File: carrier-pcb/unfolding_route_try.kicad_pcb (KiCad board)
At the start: 2 copper layers, 66 parts, among them J1 USB_C_Receptacle_USB2.0, J2 Conn_01x04_Female, J3 CONN_1-338068-8_TYC, U1 TCA9548APWR, U10 DRV2605LDGS, U11 DRV2605LDGS, U12 BMX160, U2 TCA9548APWR, U3 DRV2605LDGS, U4 DRV2605LDGS, U5 DRV2605LDGS, U6 DRV2605LDGS, U7 DRV2605LDGS, U8 DRV2605LDGS, U9 DRV2605LDGS

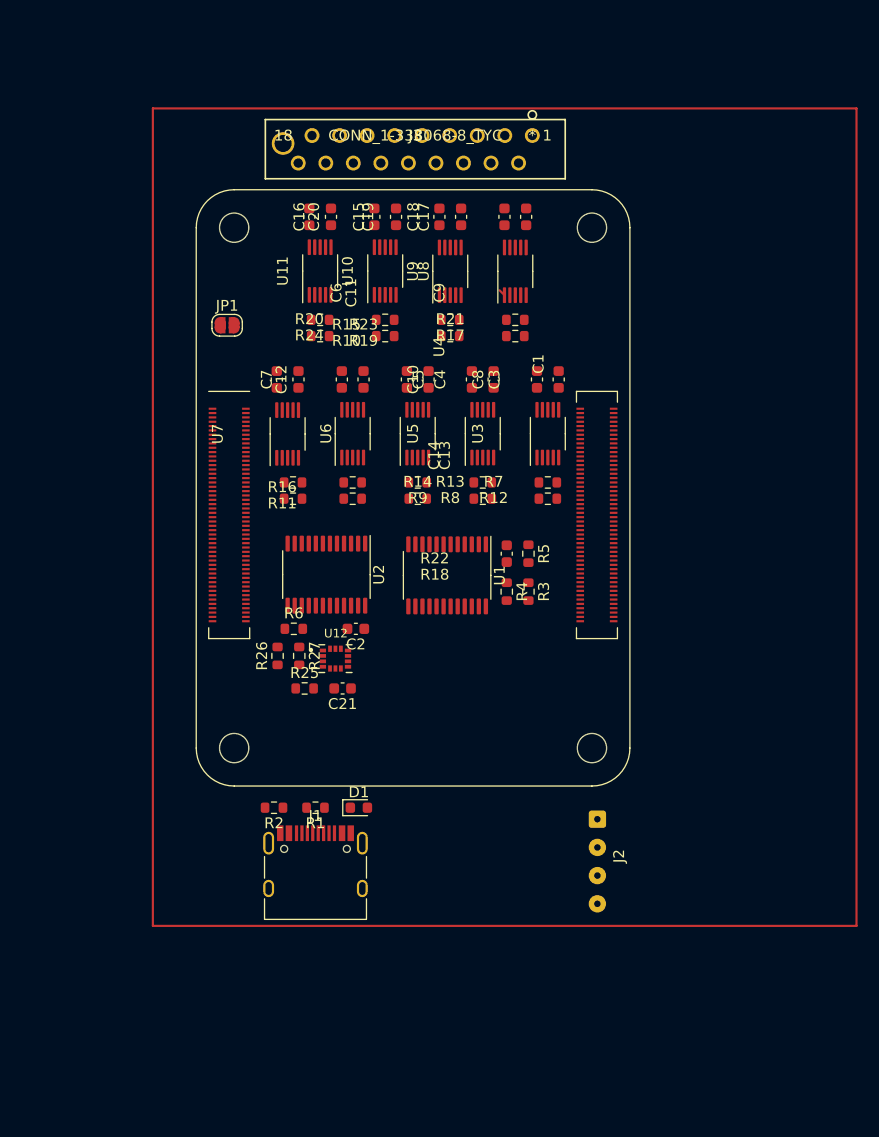
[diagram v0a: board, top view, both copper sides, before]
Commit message: Add 3rd_party_libs folder and place footrpints and symbols. Place bmx160 and TE IDC connector. Add route_try file to try out routing.
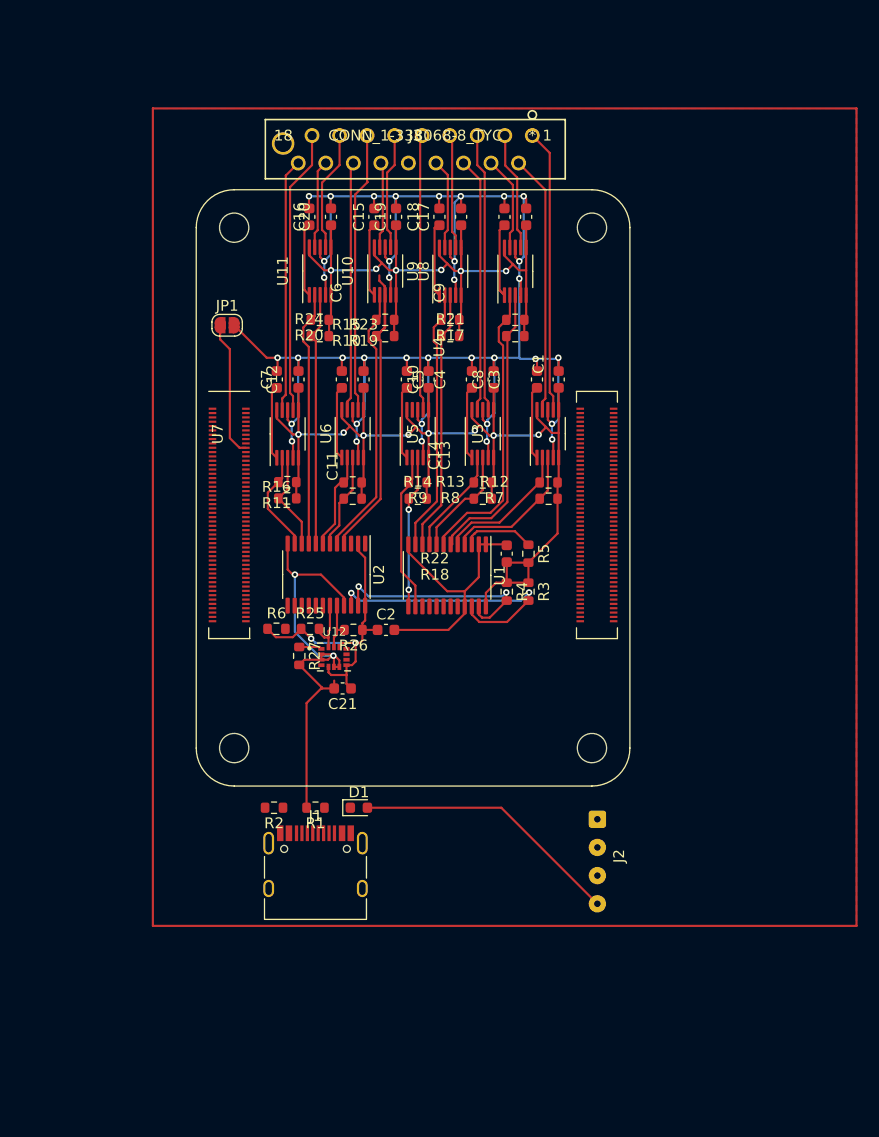
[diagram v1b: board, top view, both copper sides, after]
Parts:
- moved R26 7.40 mm to (130.0, 76.1), turned to 180 degrees
- moved R25 5.52 mm to (126.0, 76.0)
- moved C2 2.78 mm to (133.0, 76.1), turned to 0 degrees
- moved R6 1.60 mm to (122.9, 76.0)
- moved R12 1.50 mm to (148.0, 62.5)
- moved R7 1.50 mm to (148.0, 64.0)
- moved R20 1.50 mm to (126.9, 49.0)
- moved R24 1.50 mm to (126.9, 47.5)
- moved R11 0.53 mm to (123.9, 64.0)
- moved R16 0.53 mm to (123.9, 62.5)
- moved U12 0.21 mm to (128.2, 78.6)
- turned C11 to 90 degrees
- turned C12 to 90 degrees
- turned C19 to 90 degrees
- turned C20 to 90 degrees
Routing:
- net GND: track 0.00 -> 252.3 mm, vias 0 -> 38
- net +3V3: track 0.00 -> 208.9 mm, vias 0 -> 16
- net SDA6: track 0.00 -> 31.0 mm
- net SCL2: track 0.00 -> 27.1 mm
- net SDA2: track 0.00 -> 26.8 mm
- net M9+: track 0.00 -> 26.3 mm
- net M1+: track 0.00 -> 26.1 mm
- net SCL: track 0.00 -> 26.0 mm, vias 0 -> 2
- net M7+: track 0.00 -> 25.9 mm
- net M3+: track 0.00 -> 25.7 mm
- net M5+: track 0.00 -> 25.5 mm
- net SCL6: track 0.00 -> 25.2 mm
- net +5V: track 0.00 -> 24.9 mm
- net SCL4: track 0.00 -> 24.4 mm
- net SDA4: track 0.00 -> 24.0 mm
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- added copper zone on B.Cu, net GND

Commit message: Route everything in route_try file
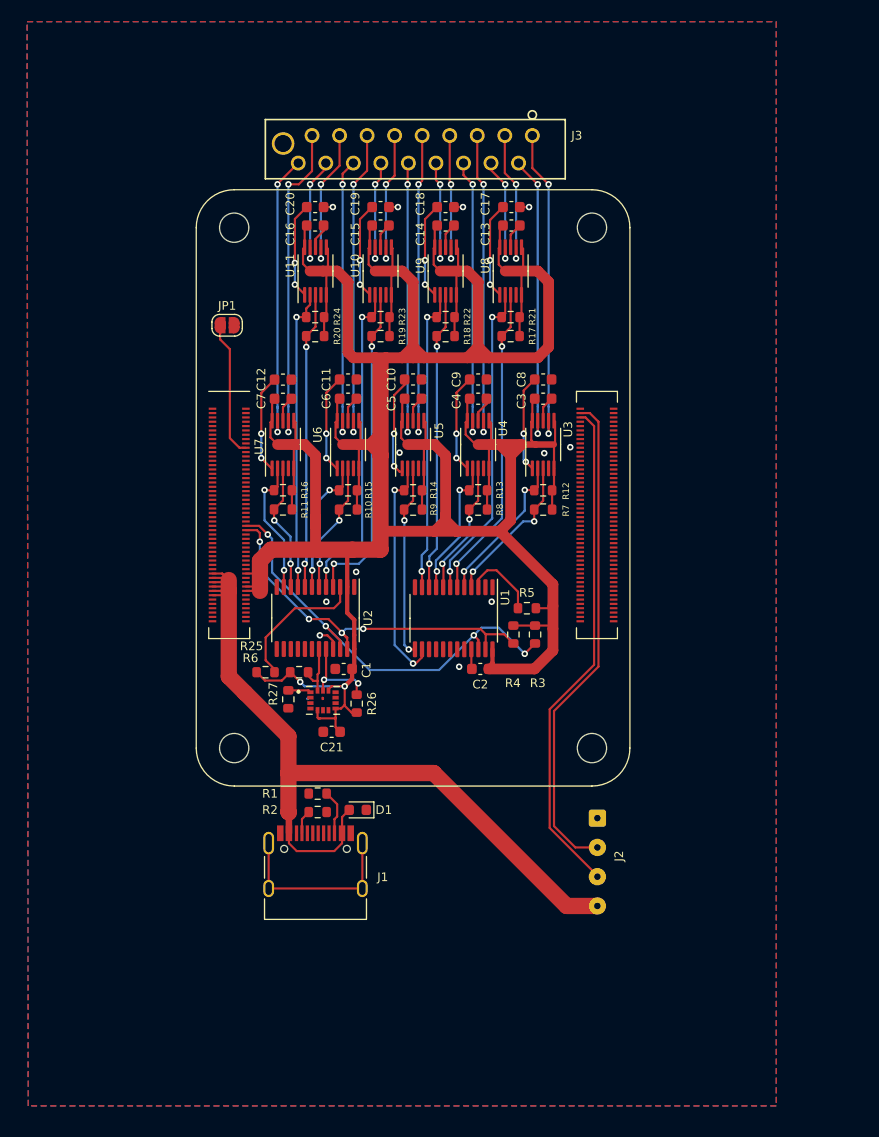
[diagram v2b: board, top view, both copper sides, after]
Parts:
- J3: value CONN_1-338068-8_TYC -> 1-338068-8
- moved C1 18.4 mm to (129.1, 79.7), turned to 180 degrees
- moved C2 9.42 mm to (141.7, 79.7), turned to 180 degrees
- moved R26 6.81 mm to (130.3, 82.9), turned to 90 degrees
- moved R5 5.03 mm to (146.0, 74.1), turned to 180 degrees
- moved C21 4.12 mm to (128.0, 85.5)
- moved R25 4.12 mm to (125.0, 80.0)
- moved R27 4.12 mm to (124.0, 82.5)
- moved R6 4.12 mm to (121.9, 80.0)
- moved U2 4.12 mm to (126.5, 75.0)
- moved U12 4.12 mm to (127.2, 82.6)
- moved R2 4.04 mm to (126.7, 92.9), turned to 0 degrees
- moved R3 4.00 mm to (146.8, 76.5)
- moved R4 4.00 mm to (144.8, 76.5)
- moved U1 4.00 mm to (139.2, 75.0)
- moved C7 2.29 mm to (123.5, 54.8), turned to 0 degrees
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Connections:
- U5 pad 9: M5-. -> M5-
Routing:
- net GND: track 252.3 -> 28.7 mm, vias 38 -> 12
- net +3V3: track 208.9 -> 342.2 mm, vias 16 -> 2
- net +5V: track 24.9 -> 78.8 mm
- net USB_D+: track 0.00 -> 46.6 mm
- net USB_D-: track 0.00 -> 45.8 mm
- net M5-: track 0.00 -> 25.9 mm, vias 0 -> 2
- net unconnected-(J1-PadS1): track 0.00 -> 17.0 mm
- net SCL: track 26.0 -> 41.2 mm, vias 2 -> 4
- net SDA: track 20.8 -> 35.1 mm, vias 2 -> 4
- net Net-(R6-Pad2): track 0.00 -> 13.2 mm
- net SCL7: track 9.05 -> 18.1 mm, vias 0 -> 2
- net SCL5: track 14.7 -> 21.5 mm, vias 0 -> 2
- net SCL6: track 25.2 -> 30.4 mm, vias 0 -> 2
- net SDA8: track 23.5 -> 28.3 mm, vias 0 -> 2
- net SCL8: track 23.6 -> 28.1 mm, vias 0 -> 2
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- added copper zone on F.Cu, net GND

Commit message: New routing
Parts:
- added J4: Conn_01x01_Female, Connector_Wire:SolderWirePad_1x01_SMD_1x2mm, F.Cu at (146.1, 89.0)
- added J5: Conn_01x01_Female, Connector_Wire:SolderWirePad_1x01_SMD_1x2mm, F.Cu at (147.5, 89.0)
- added J6: Conn_01x01_Female, Connector_Wire:SolderWirePad_1x01_SMD_1x2mm, F.Cu at (142.7, 89.0)
- J2: value Conn_01x04_Female -> Conn_01x01_Female; footprint Connector_Wire:SolderWire-0.1sqmm_1x04_P3.6mm_D0.4mm_OD1mm -> Connector_Wire:SolderWirePad_1x01_SMD_1x2mm
- moved C21 15.8 mm to (143.8, 84.8), turned to -90 degrees
- moved U12 14.0 mm to (141.0, 84.9)
- moved R27 13.7 mm to (137.6, 84.1), turned to 180 degrees
- moved R25 12.8 mm to (137.6, 82.6)
- moved R6 12.5 mm to (129.8, 70.2), turned to 180 degrees
- moved R26 10.4 mm to (140.7, 82.6), turned to 180 degrees
- moved J2 8.78 mm to (144.1, 89.0), turned to 180 degrees
- moved R2 2.50 mm to (124.2, 92.8), turned to 180 degrees
- moved R1 2.50 mm to (124.2, 91.3)
- moved D1 1.56 mm to (128.9, 92.1), turned to -90 degrees
- moved JP1 1.17 mm to (119.2, 48.8)
- moved C17 0.30 mm to (144.6, 36.8)
- moved C18 0.30 mm to (138.5, 36.8)
- moved C19 0.30 mm to (132.5, 36.8)
- moved C20 0.30 mm to (126.5, 36.8)
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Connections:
- J2 pad 1: GND -> +5V
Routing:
- net USB_D+: track 46.6 -> 0.00 mm
- net USB_D-: track 45.8 -> 0.00 mm
- net +3V3: track 342.2 -> 366.8 mm
- net GND: track 28.7 -> 49.8 mm, vias 12 -> 75
- net +5V: track 78.8 -> 62.1 mm
- net SDA_bmx160: track 5.28 -> 18.8 mm
- net Net-(R6-Pad2): track 13.2 -> 1.95 mm
- net SCL_bmx160: track 8.33 -> 19.2 mm, vias 2 -> 0
- net SCL7: track 18.1 -> 12.3 mm, vias 2 -> 0
- net SDA: track 35.1 -> 38.5 mm
- net SCL: track 41.2 -> 39.0 mm
- net SCL1: track 15.1 -> 13.8 mm, vias 2 -> 0
- net SDA2: track 29.1 -> 30.2 mm
- net Net-(J1-PadB5): track 4.16 -> 5.24 mm
- net SDA4: track 27.6 -> 28.6 mm
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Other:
- board outline added: 57 x 78.5 mm

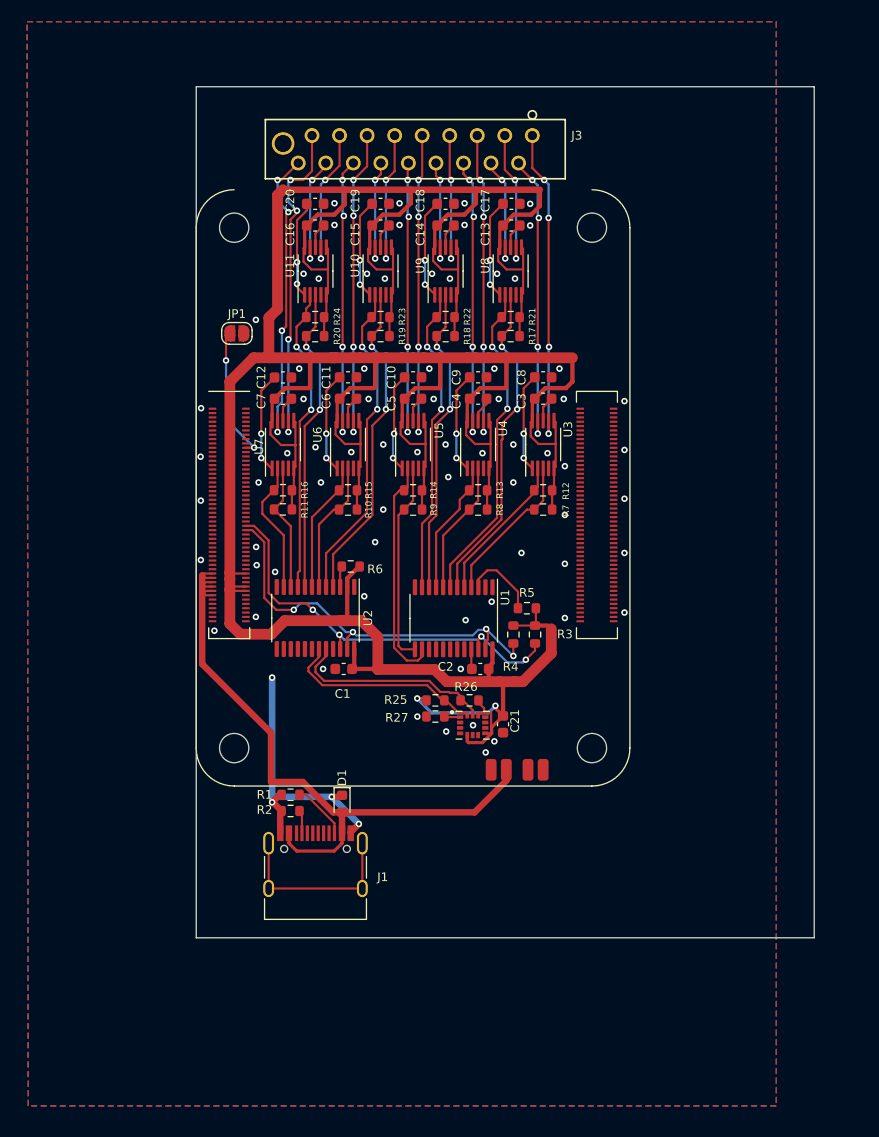
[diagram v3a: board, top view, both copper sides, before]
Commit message: finish new routing with diff pair. export stp file.
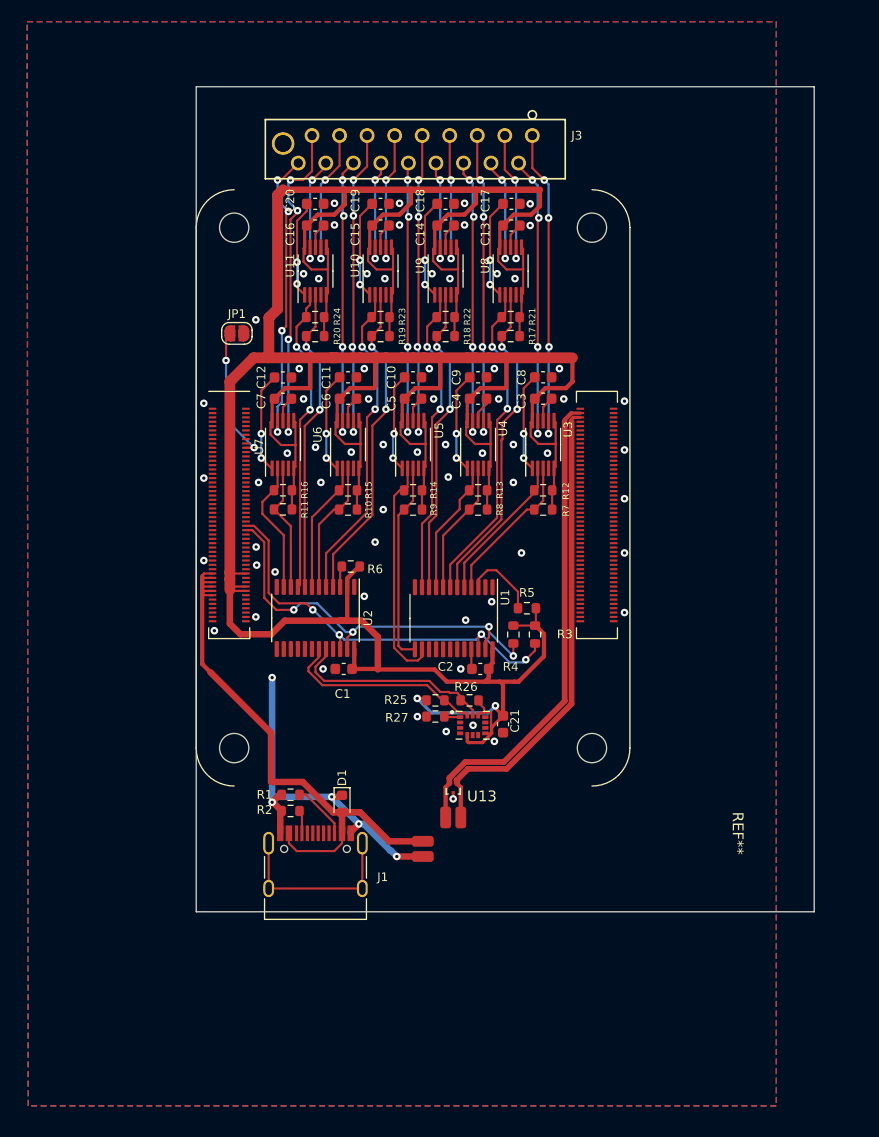
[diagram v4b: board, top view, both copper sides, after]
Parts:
- added REF**: SteckerMicro-USB30-gewinkelt, own:SteckerMicro-USB30-gewinkelt, F.Cu at (164.9, 94.9)
- added U13: TPD2EUSB30, Package_TO_SOT_SMD:Texas_DRT-3, F.Cu at (139.2, 90.7)
- moved J6 10.2 mm to (136.4, 97.0), turned to -90 degrees
- moved J2 10.1 mm to (136.4, 95.6), turned to -90 degrees
- moved J5 10.0 mm to (138.5, 93.4), turned to 0 degrees
- moved J4 7.60 mm to (139.9, 93.4), turned to 0 degrees
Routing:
- net USB_D-: track 0.00 -> 44.9 mm
- net USB_D+: track 0.00 -> 44.1 mm
- net +5V: track 62.1 -> 53.3 mm
- net GND: track 49.8 -> 57.6 mm, vias 75 -> 71
- net +3V3: track 366.8 -> 364.7 mm
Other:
- board size 57 x 78.5 mm -> 57 x 76.1 mm

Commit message: reroute usb traces. make motor traces thicker. small changes
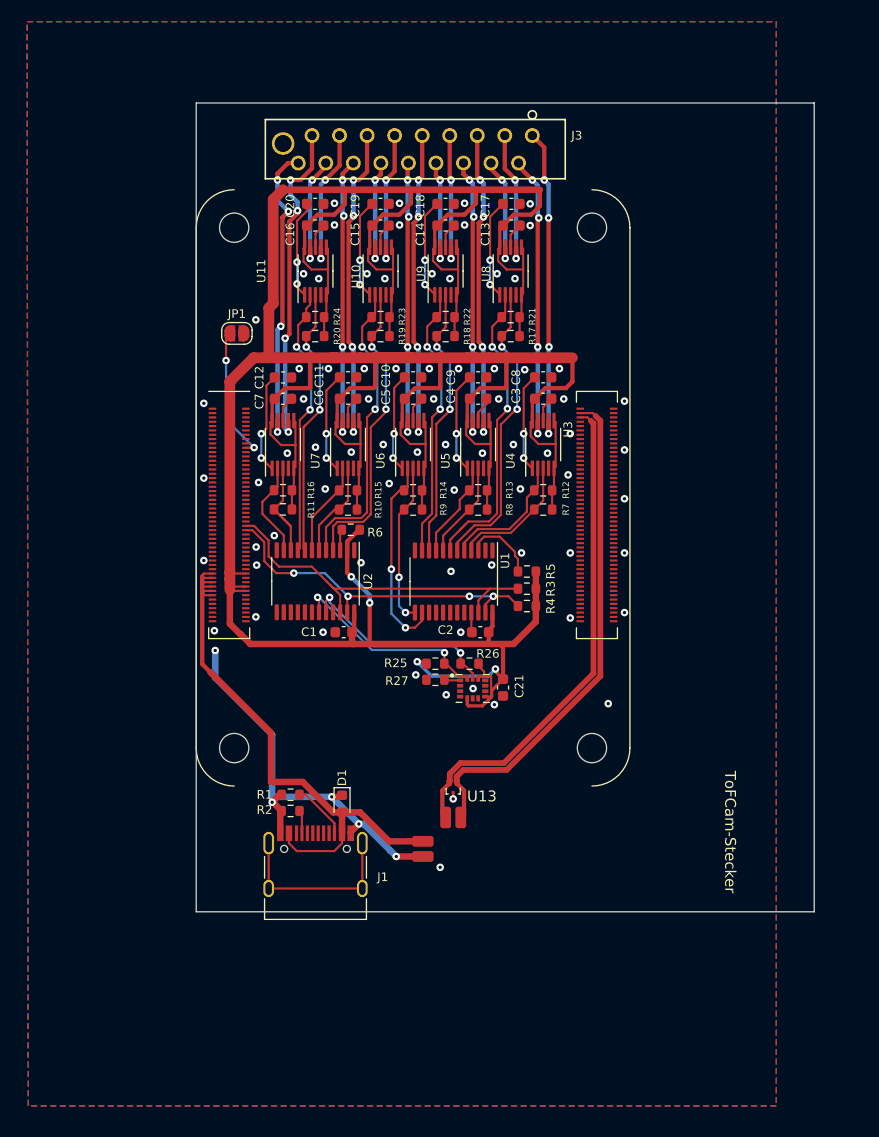
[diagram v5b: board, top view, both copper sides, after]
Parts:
- ToFCam-Stecker: renamed from REF**; value SteckerMicro-USB30-gewinkelt -> ToFCam-Stecker
- moved R3 4.29 mm to (146.0, 72.3), turned to 180 degrees
- moved C1 3.39 mm to (129.1, 76.3)
- moved C2 3.39 mm to (141.7, 76.3)
- moved C21 3.39 mm to (143.8, 81.4)
- moved R27 3.39 mm to (137.6, 80.7)
- moved R6 3.39 mm to (129.8, 66.9)
- moved U1 3.39 mm to (139.2, 71.6)
- moved U12 3.39 mm to (141.0, 81.5)
- moved U2 3.39 mm to (126.5, 71.6)
- moved R25 3.39 mm to (137.6, 79.2)
- moved R26 3.39 mm to (140.7, 79.2)
- moved R5 3.39 mm to (146.0, 70.7)
- moved R4 2.91 mm to (146.0, 73.9), turned to 180 degrees
- moved J4 1.40 mm to (138.5, 93.4)
- moved J5 1.40 mm to (139.9, 93.4)
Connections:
- U13 pad 1: USB_D+ -> USB_D-
- U13 pad 2: USB_D- -> USB_D+
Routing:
- net SDA: track 39.0 -> 32.3 mm
- net SCL: track 39.3 -> 33.9 mm, vias 4 -> 0
- net GND: track 57.6 -> 62.2 mm, vias 71 -> 80
- net SDA5: track 18.6 -> 15.0 mm, vias 0 -> 2
- net SCL7: track 12.3 -> 8.72 mm
- net SDA7: track 12.3 -> 8.89 mm
- net SCL9: track 12.3 -> 8.95 mm
- net SCL8: track 28.5 -> 25.1 mm
- net SDA3: track 12.3 -> 8.91 mm
- net SCL4: track 28.7 -> 25.3 mm
- net SCL3: track 12.4 -> 8.97 mm
- net SDA4: track 28.6 -> 25.4 mm
- net SDA8: track 28.4 -> 25.3 mm
- net SCL5: track 21.2 -> 18.6 mm, vias 0 -> 2
- net SDA2: track 30.2 -> 27.7 mm
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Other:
- board size 57 x 76.1 mm -> 57 x 74.6 mm

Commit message: add roundings, add BOM
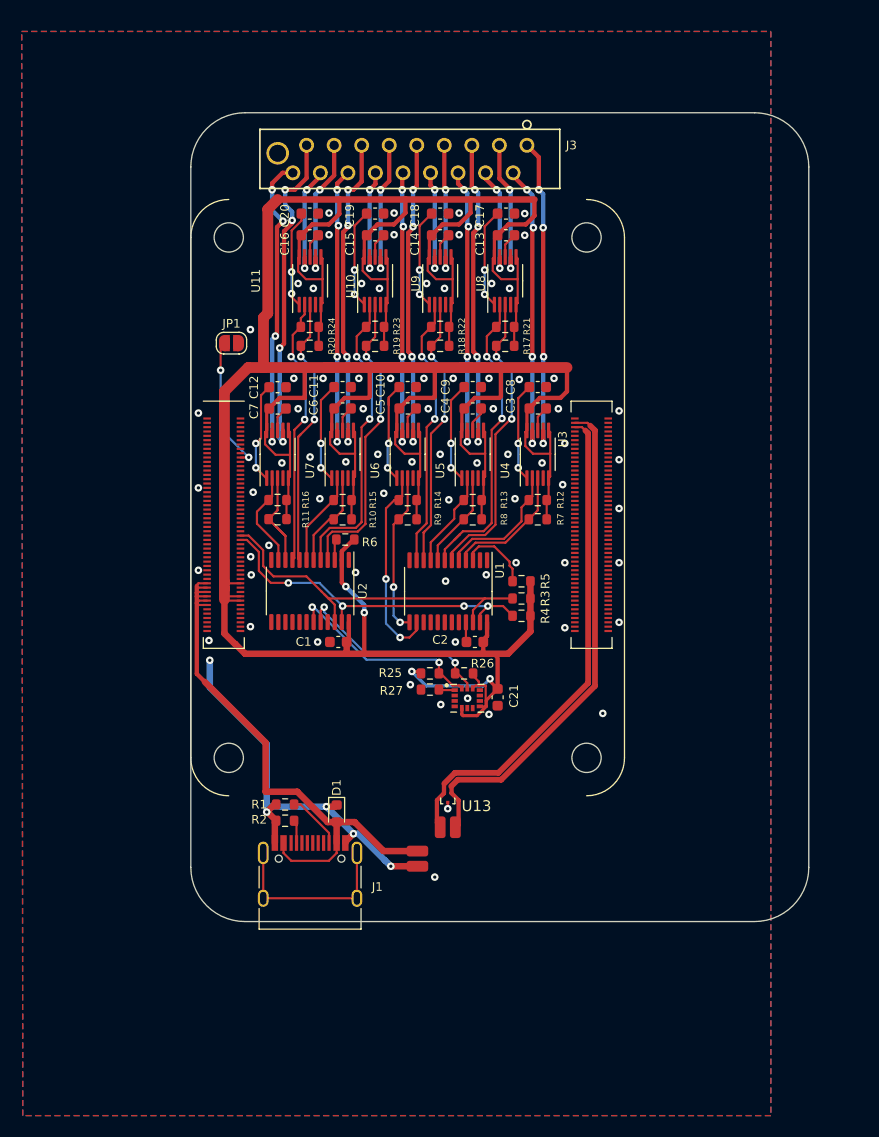
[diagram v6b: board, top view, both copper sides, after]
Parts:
- moved ToFCam-Stecker 1.10 mm to (164.6, 95.9)
- moved C1 1.03 mm to (128.6, 77.2)
- moved C10 1.03 mm to (135.0, 53.7)
- moved C11 1.03 mm to (129.0, 53.7)
- moved C12 1.03 mm to (123.0, 53.7)
- moved C13 1.03 mm to (144.1, 39.7)
- moved C14 1.03 mm to (138.0, 39.7)
- moved C15 1.03 mm to (132.0, 39.7)
- moved C16 1.03 mm to (126.0, 39.7)
- moved C17 1.03 mm to (144.1, 37.7)
- moved C18 1.03 mm to (138.0, 37.7)
- moved C19 1.03 mm to (132.0, 37.7)
- moved C2 1.03 mm to (141.2, 77.2)
- moved C20 1.03 mm to (126.0, 37.7)
- moved C8 1.03 mm to (147.0, 53.7)
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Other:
- outline, holes or cut-outs redrawn
